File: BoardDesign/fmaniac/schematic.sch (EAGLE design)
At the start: 20 parts, among them U1 ATMEGA168MLF, X1 STEREOJACK

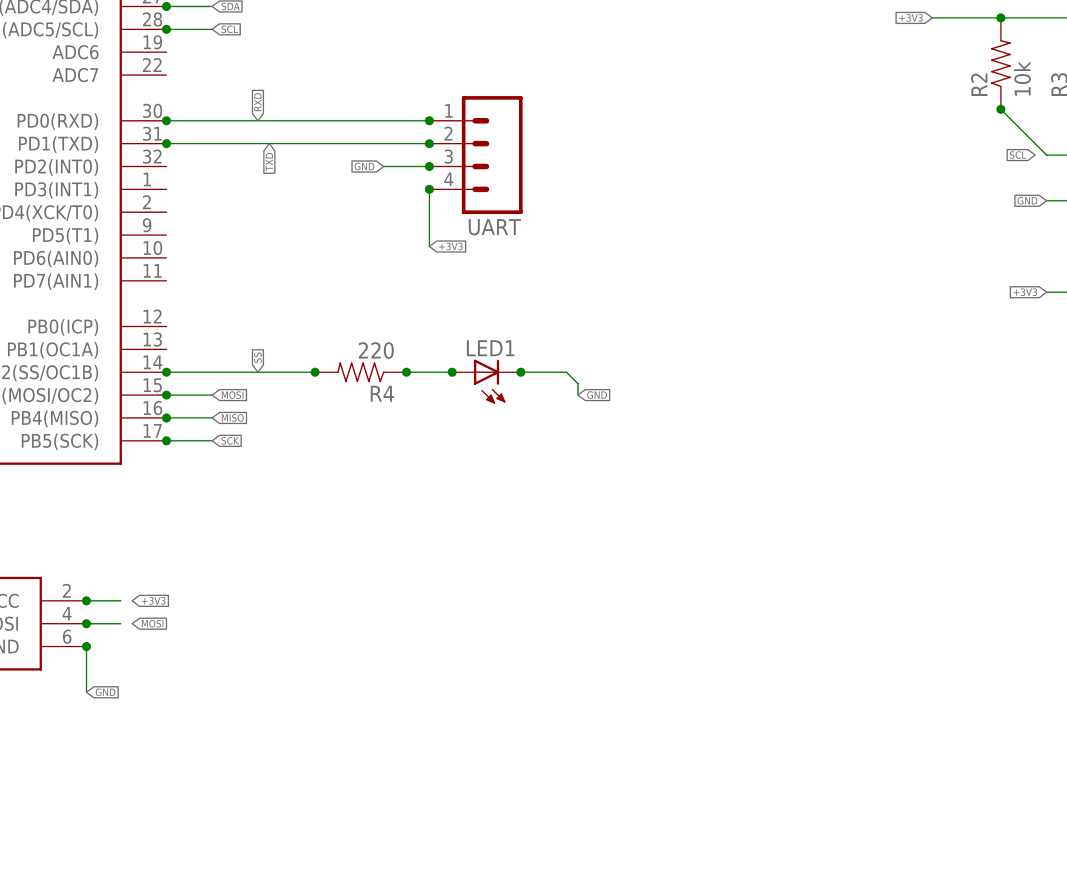
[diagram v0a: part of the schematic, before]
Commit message: Normal Push, Interrupt Button Added.
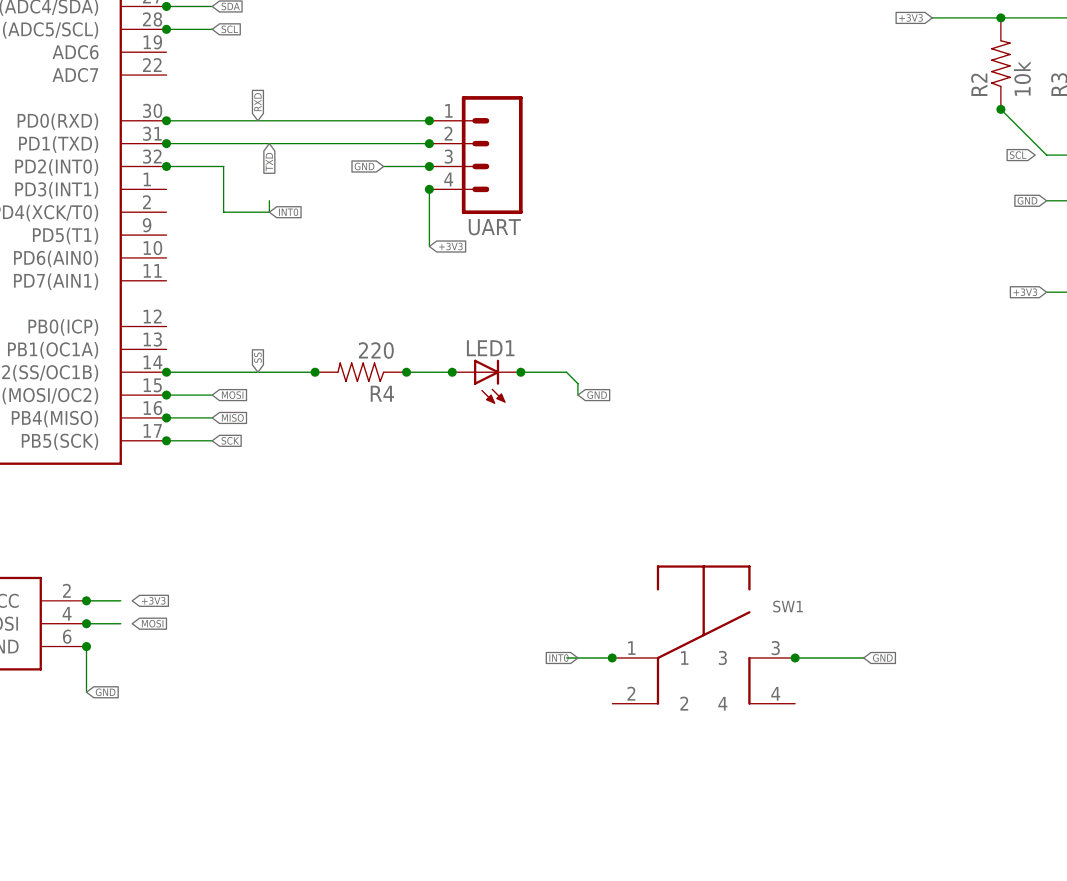
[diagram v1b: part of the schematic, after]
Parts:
- added SW1: (no value), libraryPart:TAC-SOFT
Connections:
- new net INT0: SW1.1, U1.PD2(INT0)
- net GND: now also SW1.3
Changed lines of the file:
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@@
 <part name="C7" library="weatherpilot_lbr" deviceset="CAP" device="0402-CAP" value="220nF"/>
 <part name="TP1" library="testpad" deviceset="PTR1" device="TP20SQ"/>
+<part name="SW1" library="libraryPart" deviceset="TAC-SOFT" device=""/>
 </parts>
 <sheets>
@@
 <instance part="C7" gate="G$1" x="275.59" y="180.34" rot="R270"/>
 <instance part="TP1" gate="G$1" x="257.81" y="212.09" rot="R180"/>
+<instance part="SW1" gate="G$1" x="172.72" y="134.62"/>
 </instances>
 <busses>
@@
 <label x="331.47" y="193.04" size="0.8128" layer="95" xref="yes"/>
 </segment>
+<segment>
+<pinref part="SW1" gate="G$1" pin="3"/>
+<junction x="182.88" y="134.62"/>
+<wire x1="182.88" y1="134.62" x2="190.5" y2="134.62" width="0.1524" layer="91"/>
+<label x="190.5" y="134.62" size="0.8128" layer="95" xref="yes"/>
+</segment>
 </net>
 <net name="+5V" class="0">
@@
 </segment>
 </net>
+<net name="INT0" class="0">
+<segment>
+<pinref part="U1" gate="G$1" pin="PD2(INT0)"/>
+<junction x="113.03" y="189.23"/>
+<wire x1="113.03" y1="189.23" x2="119.38" y2="189.23" width="0.1524" layer="91"/>
+<wire x1="119.38" y1="189.23" x2="119.38" y2="184.15" width="0.1524" layer="91"/>
+<wire x1="119.38" y1="184.15" x2="124.46" y2="184.15" width="0.1524" layer="91"/>
+<wire x1="124.46" y1="184.15" x2="124.46" y2="185.42" width="0.1524" layer="91"/>
+<label x="124.46" y="184.15" size="0.8128" layer="95" xref="yes"/>
+</segment>
+<segment>
+<pinref part="SW1" gate="G$1" pin="1"/>
+<junction x="162.56" y="134.62"/>
+<wire x1="162.56" y1="134.62" x2="157.48" y2="134.62" width="0.1524" layer="91"/>
+<label x="158.75" y="134.62" size="0.8128" layer="95" rot="R180" xref="yes"/>
+</segment>
+</net>
